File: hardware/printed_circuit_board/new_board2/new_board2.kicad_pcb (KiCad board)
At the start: 2 copper layers, 80.7 x 123.4 mm, 53 parts, among them CON1 BARREL_JACK, J1 Conn_01x14_Socket, J2 Conn_01x14_Socket, P1 Conn_01x02, P10 D6, P11 D8, P12 A2, P13 Conn_01x02, P14 Conn_01x02, P15 Conn_01x02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

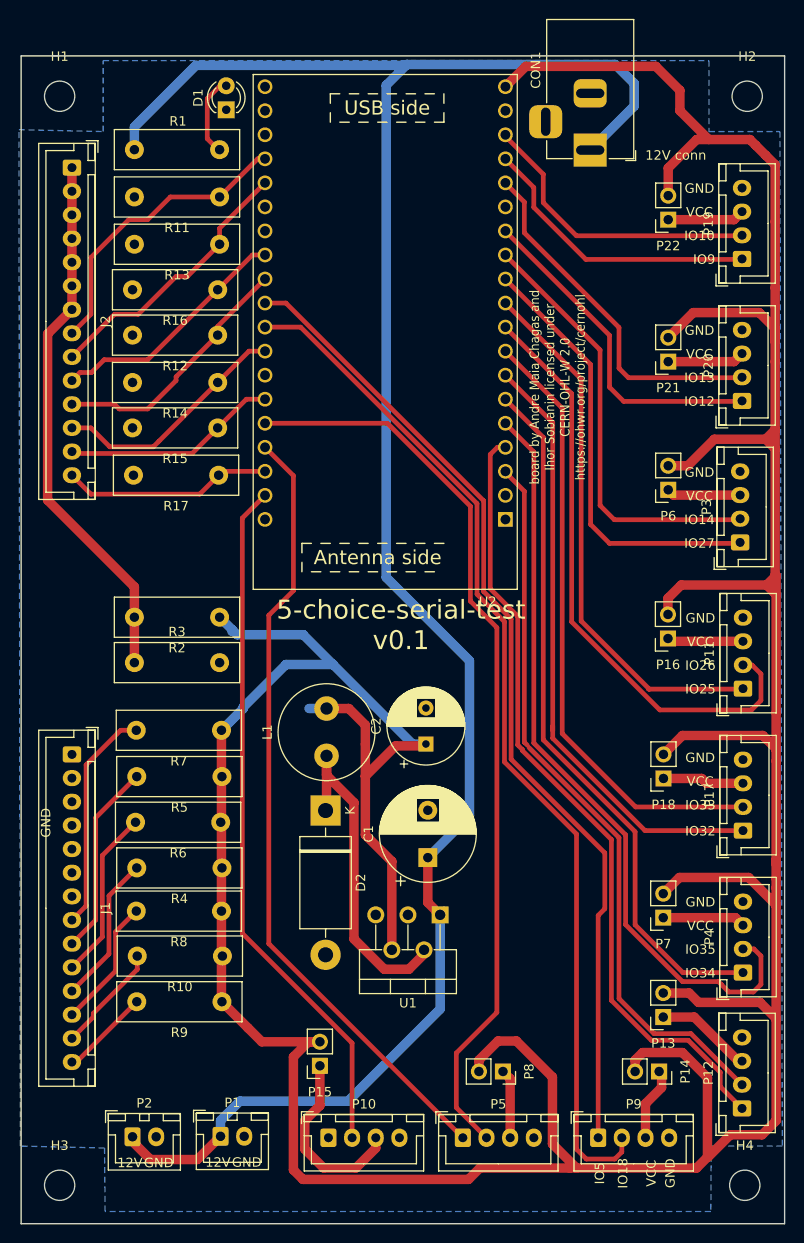
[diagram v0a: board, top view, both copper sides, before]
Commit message: simplify PCB, making stable connections for LEDs using a ULN2003, remove jumpers, THIS IS STILL UNTESTED!
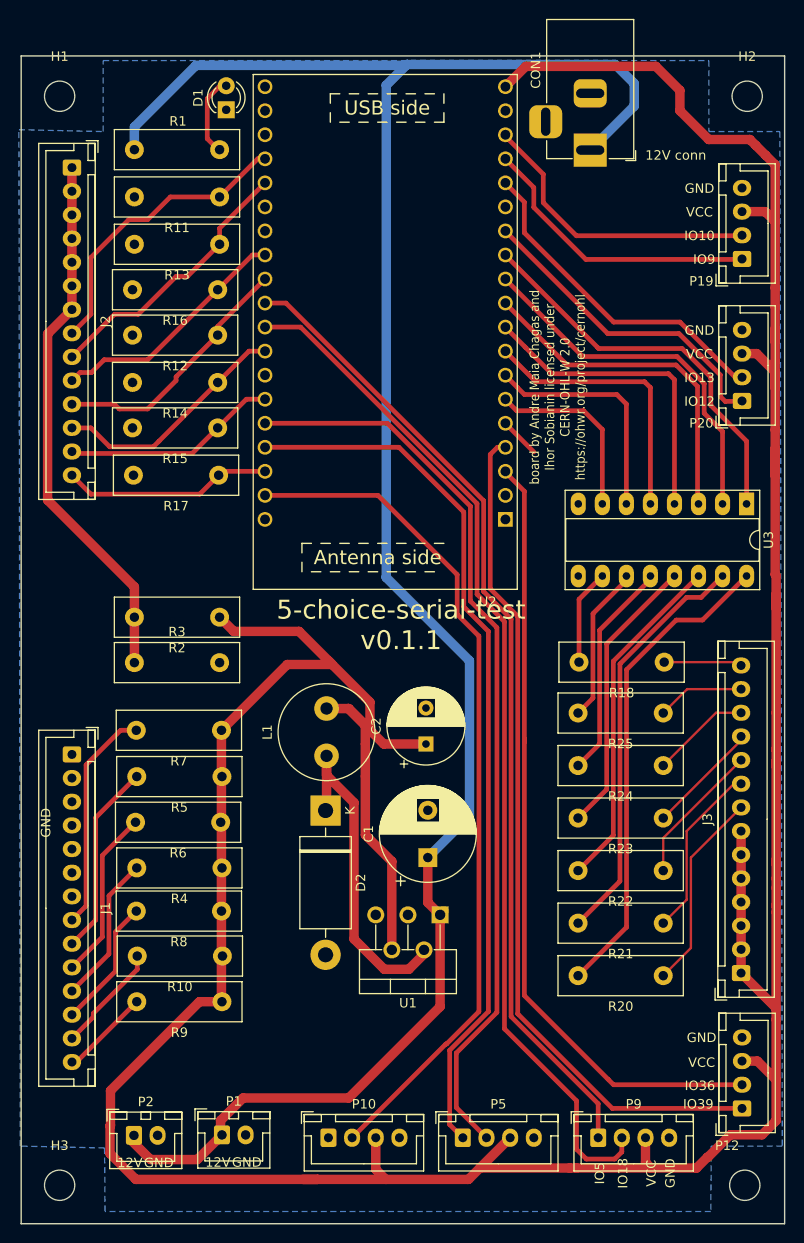
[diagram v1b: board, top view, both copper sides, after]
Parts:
- removed P11: D8, Connector_JST:JST_XH_B4B-XH-A_1x04_P2.50mm_Vertical
- removed P13, P14, P15, P16, P18, P21, P22, P6, P7, P8: Conn_01x02, Connector_PinSocket_2.54mm:PinSocket_1x02_P2.54mm_Vertical
- removed P17: A3, Connector_JST:JST_XH_B4B-XH-A_1x04_P2.50mm_Vertical
- removed P3: D7, Connector_JST:JST_XH_B4B-XH-A_1x04_P2.50mm_Vertical
- removed P4: A1, Connector_JST:JST_XH_B4B-XH-A_1x04_P2.50mm_Vertical
- added J3: Conn_01x14_Socket, Connector_JST:JST_XH_B14B-XH-A_1x14_P2.50mm_Vertical, F.Cu at (211.7, 137.6)
- added R18: 560, Resistor_THT:R_Box_L13.0mm_W4.0mm_P9.00mm, F.Cu at (203.6, 104.8)
- added R20: 560, Resistor_THT:R_Box_L13.0mm_W4.0mm_P9.00mm, F.Cu at (203.5, 137.9)
- added R21: 560, Resistor_THT:R_Box_L13.0mm_W4.0mm_P9.00mm, F.Cu at (203.5, 132.3)
- added R22: 560, Resistor_THT:R_Box_L13.0mm_W4.0mm_P9.00mm, F.Cu at (203.5, 126.8)
- added R23: 560, Resistor_THT:R_Box_L13.0mm_W4.0mm_P9.00mm, F.Cu at (203.5, 121.2)
- added R24: 560, Resistor_THT:R_Box_L13.0mm_W4.0mm_P9.00mm, F.Cu at (203.5, 115.7)
- added R25: 560, Resistor_THT:R_Box_L13.0mm_W4.0mm_P9.00mm, F.Cu at (203.5, 110.1)
- added U3: ULN2003, Package_DIP:DIP-16_W7.62mm_Socket_LongPads, F.Cu at (212.3, 88.0)
- moved P1 0.21 mm to (156.8, 154.7)
- moved P2 0.21 mm to (147.6, 154.8)
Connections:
- P10 pad 3: Net-(P10-Pin_3) -> +5V
- P12 pad 3: Net-(P12-Pin_3) -> +5V
- P19 pad 3: Net-(P19-Pin_3) -> +5V
- P20 pad 3: Net-(P20-Pin_3) -> +5V
- P5 pad 3: Net-(P5-Pin_3) -> +5V
- P9 pad 3: Net-(P14-Pin_1) -> +5V
- U2 pad 10: D8-3 -> Net-(U2-IO26)
- U2 pad 11: D7-4 -> Net-(U2-IO27)
- U2 pad 12: D7-3 -> Net-(U2-IO14)
- U2 pad 6: A1-3 -> Net-(U2-IO35)
- U2 pad 7: A3-3 -> Net-(U2-IO32)
- U2 pad 8: A3-4 -> Net-(U2-IO33)
- U2 pad 9: D8-4 -> Net-(U2-IO25)
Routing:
- net A1-4: track 81.0 -> 4.24 mm
- net A1-3: track 75.0 -> 0.00 mm
- net +5V: track 462.5 -> 394.8 mm
- net A3-4: track 65.2 -> 0.00 mm
- net A3-3: track 65.0 -> 0.00 mm
- net D8-4: track 63.4 -> 0.00 mm
- net D8-3: track 57.1 -> 0.00 mm
- net Net-(U3-O1): track 0.00 -> 51.2 mm
- net D7-4: track 46.5 -> 0.00 mm
- net D7-3: track 46.2 -> 0.00 mm
- net Net-(U3-O2): track 0.00 -> 43.9 mm
- net Net-(U2-IO14): track 0.00 -> 42.0 mm
- net Net-(U2-IO27): track 0.00 -> 39.1 mm
- net Net-(U3-O3): track 0.00 -> 36.4 mm
- net Net-(U2-IO26): track 0.00 -> 36.4 mm
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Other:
- board text added: "5-choice-serial-test v0.1.1"
- board text added: "IO36"
- board text added: "IO39"
- board text removed: "5-choice-serial-test v0.1"
- board text removed: "IO14"
- board text removed: "IO25"
- board text removed: "IO26"
- board text removed: "IO27"
- board text removed: "IO32"
- board text removed: "IO33"
- board text removed: "IO34"
- board text removed: "IO35"
